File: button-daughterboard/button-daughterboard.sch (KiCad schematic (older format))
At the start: 0 parts

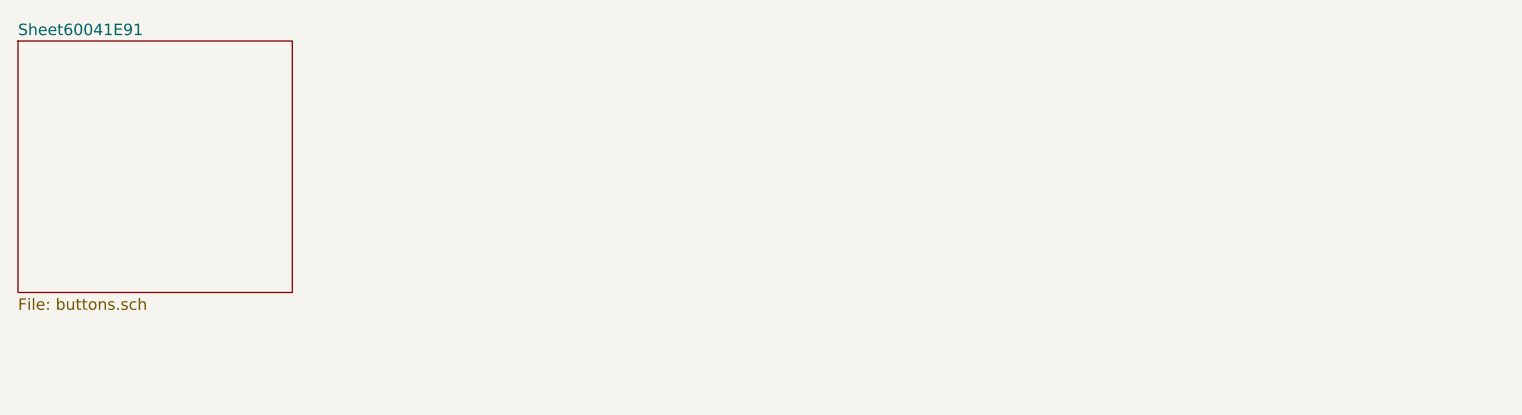
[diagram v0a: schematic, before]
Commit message: Panelize button daughterboards
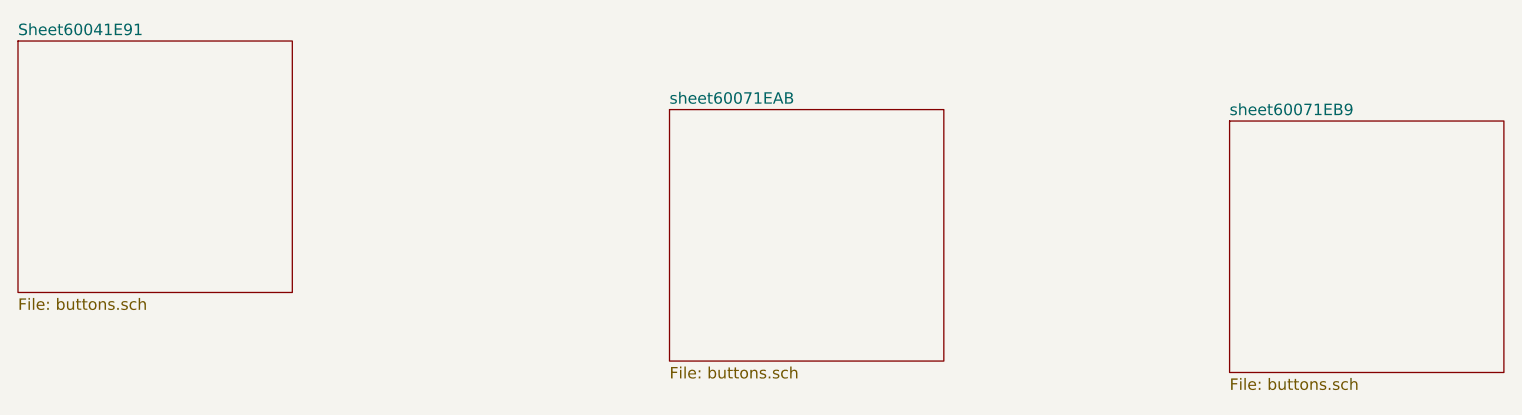
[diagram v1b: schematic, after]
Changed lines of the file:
@@
+F1 "buttons.sch" 50
+$EndSheet
+$Sheet
+S 6900 3350 1200 1100
+U 60071EAD
+F0 "sheet60071EAB" 50
+F1 "buttons.sch" 50
+$EndSheet
+$Sheet
+S 9350 3400 1200 1100
+U 60071EBB
+F0 "sheet60071EB9" 50
 F1 "buttons.sch" 50
 $EndSheet
